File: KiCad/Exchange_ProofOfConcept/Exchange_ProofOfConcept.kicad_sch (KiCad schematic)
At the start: 21 parts, among them J1 Connector_PinHeader_2.54mm:Pi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, J2 Conn_01x02, J3 Conn_01x02, J4 Conn_01x02, J5 Connector_PinHeader_2.54mm:Pi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, J6 Connector_PinHeader_2.54mm:Pi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, J7 Screw_Terminal_01x02, J8 Conn_01x03, J9 Screw_Terminal_01x08, U1 MCP23017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

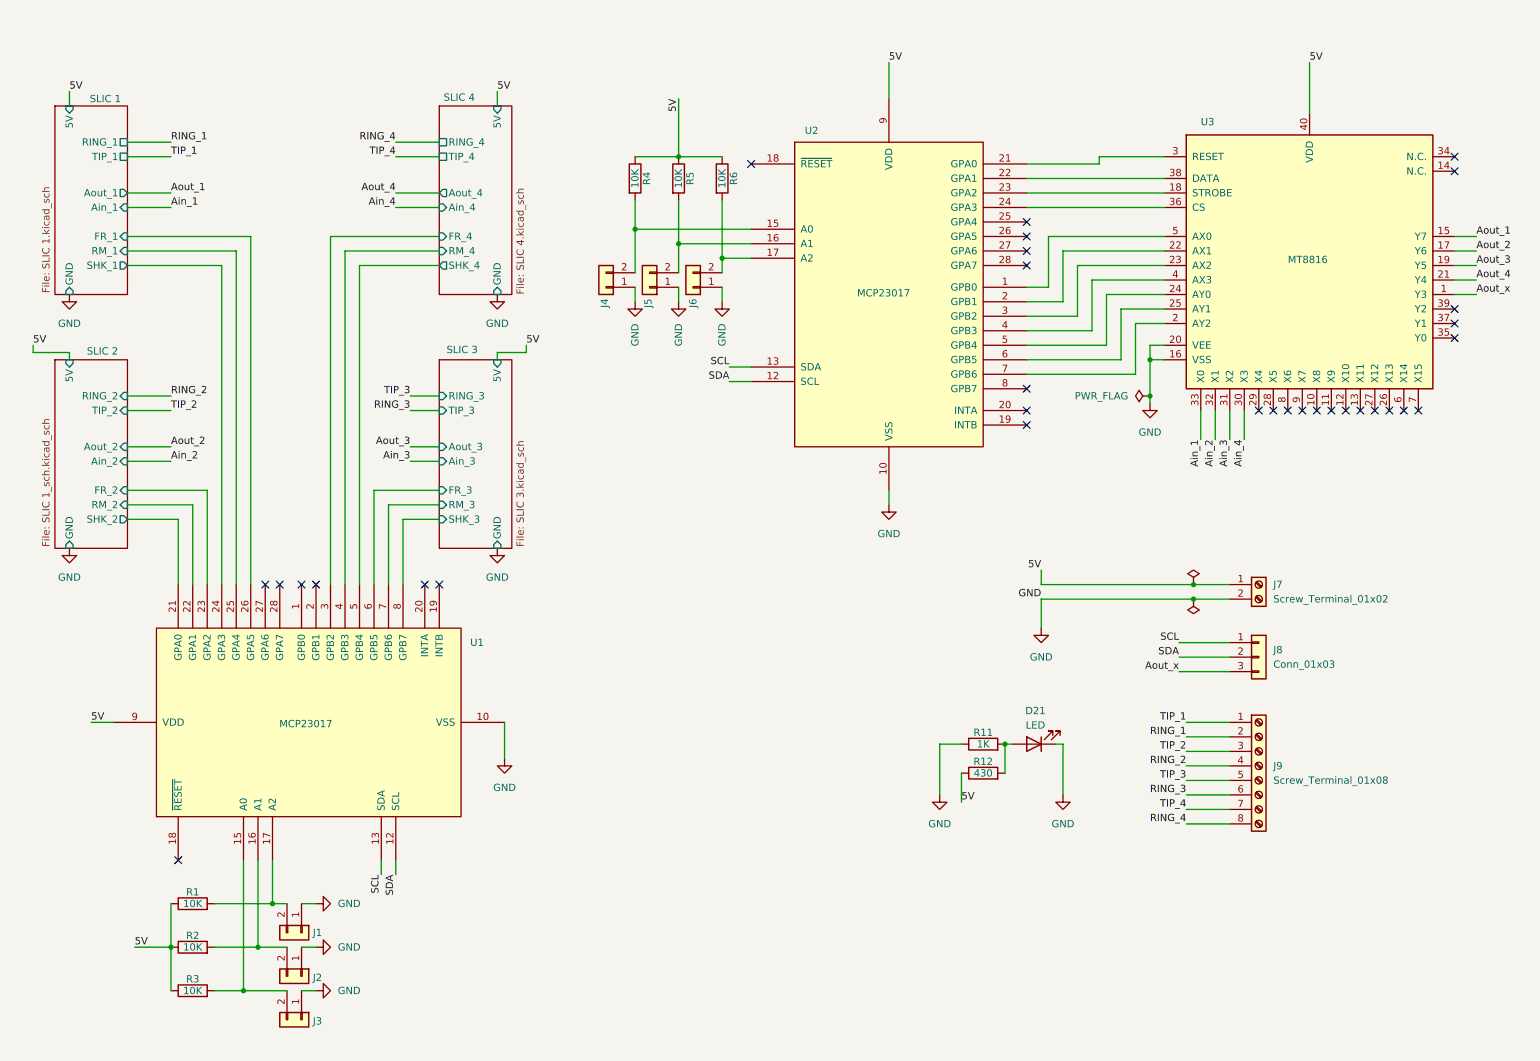
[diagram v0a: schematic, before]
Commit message: deleted:    KiCad/Exchange_ProofOfConcept/Exchange_ProofOfConcept-backups/Exchange_ProofOfConcept-2024-08-28_233227.zip 	deleted:    KiCad/Exchange_ProofOfConcept/Exchange_ProofOfConcept-backups/Exchange_ProofOfConcept-2024-08-28_234504.zip 	deleted:    KiCad/Exchange_ProofOfConcept/Exchange_ProofOfConcept-backups/Exchange_ProofOfConcept-2024-09-04_201626.zip 	deleted:    KiCad/Exchange_ProofOfConcept/Exchange_ProofOfConcept-backups/Exchange_ProofOfConcept-2024-09-04_202659.zip 	deleted:    KiCad/Exchange_ProofOfConcept/Exchange_ProofOfConcept-backups/Exchange_ProofOfConcept-2024-09-04_203703.zip 	deleted:    KiCad/Exchange_ProofOfConcept/Exchange_ProofOfConcept-backups/Exchange_ProofOfConcept-2024-09-04_204710.zip 	deleted:    KiCad/Exchange_ProofOfConcept/Exchange_ProofOfConcept-backups/Exchange_ProofOfConcept-2024-09-04_205754.zip 	deleted:    KiCad/Exchange_ProofOfConcept/Exchange_ProofOfConcept-backups/Exchange_ProofOfConcept-2024-09-05_153643.zip 	deleted:    KiCad/Exchange_ProofOfConcept/Exchange_ProofOfConcept-backups/Exchange_ProofOfConcept-2024-09-05_161017.zip 	deleted:    KiCad/Exchange_ProofOfConcept/Exchange_ProofOfConcept-backups/Exchange_ProofOfConcept-2024-09-05_162441.zip 	deleted:    KiCad/Exchange_ProofOfConcept/Exchange_ProofOfConcept-backups/Exchange_ProofOfConcept-2024-09-05_163641.zip 	deleted:    KiCad/Exchange_ProofOfConcept/Exchange_ProofOfConcept-backups/Exchange_ProofOfConcept-2024-09-06_180233.zip 	deleted:    KiCad/Exchange_ProofOfConcept/Exchange_ProofOfConcept-backups/Exchange_ProofOfConcept-2024-09-06_180943.zip 	deleted:    KiCad/Exchange_ProofOfConcept/Exchange_ProofOfConcept-backups/Exchange_ProofOfConcept-2024-09-06_182256.zip 	deleted:    KiCad/Exchange_ProofOfConcept/Exchange_ProofOfConcept-backups/Exchange_ProofOfConcept-2024-09-06_185314.zip 	deleted:    KiCad/Exchange_ProofOfConcept/Exchange_ProofOfConcept-backups/Exchange_ProofOfConcept-2024-09-06_191143.zip 	deleted:    KiCad/Exchange_ProofOfConcept/Exchange_ProofOfConcep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
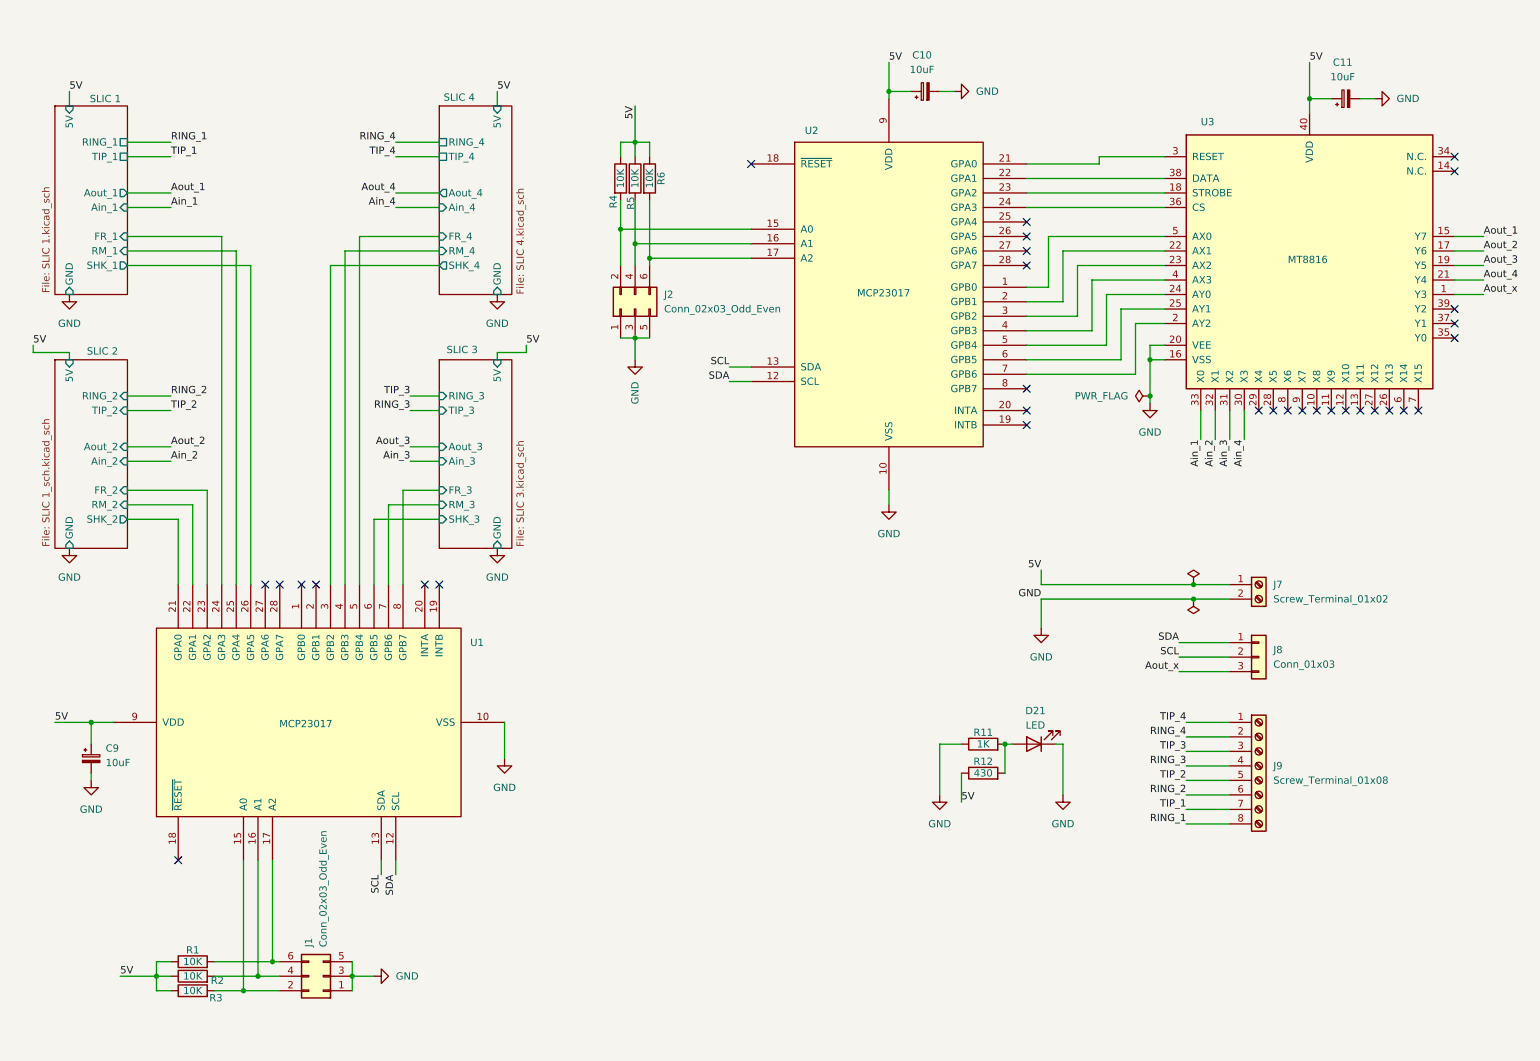
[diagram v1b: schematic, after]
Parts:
- removed J1, J5, J6: Connector_PinHeader_2.54mm:PinHeader_1x02_P2.54mm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, Connector_PinHeader_2.54mm:PinHeader_1x02_P2.54mm_Vertical, symbol Connector_Generic:Conn_01x02
- removed J2, J3, J4: Conn_01x02, Connector_PinHeader_2.54mm:PinHeader_1x02_P2.54mm_Vertical, symbol Connector_Generic:Conn_01x02
- added C10, C11, C9: 10uF, Capacitor_THT:CP_Radial_D4.0mm_P2.00mm, symbol Device:C_Polarized_Small
- added J1, J2: Conn_02x03_Odd_Even, Connector_PinHeader_2.54mm:PinHeader_2x03_P2.54mm_Vertical, symbol Connector_Generic:Conn_02x03_Odd_Even
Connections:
- net 5V: now also C10.1, C11.1, C9.1
- net GND: now also C10.2, C11.2, C9.2, J1.1 (Pin_1), J1.3 (Pin_3), J1.5 (Pin_5), J2.1 (Pin_1), J2.3 (Pin_3), J2.5 (Pin_5)
- net RING_1: now also J9.8 (Pin_8); no longer J9.2 (Pin_2)
- net RING_2: now also J9.6 (Pin_6); no longer J9.4 (Pin_4)
- net RING_3: now also J9.4 (Pin_4); no longer J9.6 (Pin_6)
- net RING_4: now also J9.2 (Pin_2); no longer J9.8 (Pin_8)
- net SCL: now also J8.2 (Pin_2); no longer J8.1 (Pin_1)
- net SDA: now also J8.1 (Pin_1); no longer J8.2 (Pin_2)
- net SLIC 1/FR_1: now also U1.24 (GPA3); no longer U1.26 (GPA5)
- net SLIC 1/SHK_1: now also U1.26 (GPA5); no longer U1.24 (GPA3)
- net SLIC 3/FR_3: now also U1.8 (GPB7); no longer U1.6 (GPB5)
- net SLIC 3/SHK_3: now also U1.6 (GPB5); no longer U1.8 (GPB7)
- net SLIC 4/FR_4: now also U1.5 (GPB4); no longer U1.3 (GPB2)
- net SLIC 4/SHK_4: now also U1.3 (GPB2); no longer U1.5 (GPB4)
- net TIP_1: now also J9.7 (Pin_7); no longer J9.1 (Pin_1)
- net TIP_2: now also J9.5 (Pin_5); no longer J9.3 (Pin_3)
- net TIP_3: now also J9.3 (Pin_3); no longer J9.5 (Pin_5)
- net TIP_4: now also J9.1 (Pin_1); no longer J9.7 (Pin_7)
- net at R2.2, U1.16 (A1): now also J1.4 (Pin_4)
- net at R3.2, U1.15 (A0): now also J1.2 (Pin_2)
- net at R5.2, U2.16 (A1): now also J2.4 (Pin_4)
- net at R4.2, U2.15 (A0): now also J2.2 (Pin_2)
- net at R1.2, U1.17 (A2): now also J1.6 (Pin_6)
- net at R6.2, U2.17 (A2): now also J2.6 (Pin_6)
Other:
- moved on the sheet: R4, R5, R6

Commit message: deleted:    KiCad/Exchange_ProofOfConcept/Exchange_ProofOfConcept-backups/Exchange_ProofOfConcept-2024-09-22_005249.zip 	new file:   KiCad/Exchange_ProofOfConcept/Exchange_ProofOfConcept-backups/Exchange_ProofOfConcept-2024-10-02_184119.zip 	modified:   KiCad/Exchange_ProofOfConcept/Exchange_ProofOfConcept.kicad_pcb 	modified:   KiCad/Exchange_ProofOfConcept/Exchange_ProofOfConcept.kicad_sch 	modified:   docs/PhoneStatusflowshart.drawio 	modified:   lib/LineStatusHandler/LineStatusHandler.cpp 	modified:   lib/LineStatusHandler/LineStatusHandler.h 	modified:   platformio.ini 	modified:   src/SHKRead.h 	modified:   src/config.h 	modified:   src/lineAction.h 	modified:   src/main.cpp
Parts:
- removed R11: 1K, Resistor_THT:R_Axial_DIN0204_L3.6mm_D1.6mm_P5.08mm_Horizontal, symbol Device:R
- R12: value 430 -> 470
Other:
- moved on the sheet: R12
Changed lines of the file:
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@@
 	)
 	(junction
-		(at 191.77 142.24)
-		(diameter 0)
-		(color 0 0 0 0)
-	)
-	(junction
 		(at 124.46 52.07)
 		(diameter 0)
@@
 	(wire
 		(pts
-			(xy 191.77 142.24) (xy 191.77 147.32)
-		)
-		(stroke
-			(width 0)
-			(type default)
-		)
-	)
-	(wire
-		(pts
 			(xy 129.54 57.15) (xy 147.32 57.15)
 		)
@@
 	(wire
 		(pts
-			(xy 180.34 142.24) (xy 180.34 151.13)
-		)
-		(stroke
-			(width 0)
-			(type default)
-		)
-	)
-	(wire
-		(pts
 			(xy 214.63 68.58) (xy 219.71 68.58)
 		)
@@
 	(wire
 		(pts
-			(xy 184.15 147.32) (xy 184.15 152.4)
+			(xy 180.34 142.24) (xy 180.34 156.21)
 		)
 		(stroke
@@
 	(wire
 		(pts
-			(xy 180.34 142.24) (xy 184.15 142.24)
+			(xy 87.63 83.82) (xy 92.71 83.82)
 		)
 		(stroke
@@
 	(wire
 		(pts
-			(xy 87.63 83.82) (xy 92.71 83.82)
+			(xy 143.51 76.2) (xy 147.32 76.2)
 		)
 		(stroke
@@
 	(wire
 		(pts
-			(xy 143.51 76.2) (xy 147.32 76.2)
+			(xy 231.14 83.82) (xy 231.14 88.9)
 		)
 		(stroke
@@
 	(wire
 		(pts
-			(xy 231.14 83.82) (xy 231.14 88.9)
+			(xy 198.12 114.3) (xy 224.79 114.3)
 		)
 		(stroke
@@
 	(wire
 		(pts
-			(xy 198.12 114.3) (xy 224.79 114.3)
+			(xy 223.52 138.43) (xy 231.14 138.43)
 		)
 		(stroke
@@
 	(wire
 		(pts
-			(xy 223.52 138.43) (xy 231.14 138.43)
+			(xy 180.34 142.24) (xy 184.15 142.24)
 		)
 		(stroke
@@
 	)
 	(label "5V"
-		(at 184.15 152.4 0)
+		(at 180.34 156.21 0)
 		(fields_autoplaced yes)
 		(effects
@@
 	(symbol
 		(lib_id "Device:R")
-		(at 187.96 147.32 90)
+		(at 187.96 142.24 90)
 		(unit 1)
 		(exclude_from_sim no)
@@
 		(dnp no)
 		(property "Reference" "R12"
-			(at 187.96 145.288 90)
+			(at 187.96 140.208 90)
 			(effects
 				(font
@@
 			)
 		)
-		(property "Value" "430"
-			(at 187.96 147.32 90)
+		(property "Value" "470"
+			(at 187.96 142.24 90)
 			(effects
 				(font
@@
 		)
 		(property "Footprint" "Resistor_THT:R_Axial_DIN0204_L3.6mm_D1.6mm_P5.08mm_Horizontal"
-			(at 187.96 149.098 90)
+			(at 187.96 144.018 90)
 			(effects
 				(font
@@
 		)
 		(property "Datasheet" "~"
-			(at 187.96 147.32 0)
+			(at 187.96 142.24 0)
 			(effects
 				(font
@@
 		)
 		(property "Description" "Resistor"
-			(at 187.96 147.32 0)
+			(at 187.96 142.24 0)
 			(effects
 				(font
@@
 	(symbol
 		(lib_id "Device:R")
-		(at 187.96 142.24 90)
-		(unit 1)
-		(exclude_from_sim no)
-		(in_bom yes)
-		(on_board yes)
-		(dnp no)
-		(property "Reference" "R11"
-			(at 187.96 140.208 90)
-			(effects
-				(font
-					(size 1.27 1.27)
-				)
-			)
-		)
-		(property "Value" "1K"
-			(at 187.96 142.24 90)
-			(effects
-				(font
-					(size 1.27 1.27)
-				)
-			)
-		)
-		(property "Footprint" "Resistor_THT:R_Axial_DIN0204_L3.6mm_D1.6mm_P5.08mm_Horizontal"
-			(at 187.96 144.018 90)
-			(effects
-				(font
-					(size 1.27 1.27)
-				)
-				(hide yes)
-			)
-		)
-		(property "Datasheet" "~"
-			(at 187.96 142.24 0)
-			(effects
-				(font
-					(size 1.27 1.27)
-				)
-				(hide yes)
-			)
-		)
-		(property "Description" "Resistor"
-			(at 187.96 142.24 0)
-			(effects
-				(font
-					(size 1.27 1.27)
-				)
-				(hide yes)
-			)
-		)
-		(pin "2"
-		)
-		(pin "1"
-		)
-		(instances
-			(project "Exchange_ProofOfConcept"
-				(path "/a3aa82f3-37b8-406c-999a-d11513c8e1fa"
-					(reference "R11")
-					(unit 1)
-				)
-			)
-		)
-	)
-	(symbol
-		(lib_id "Device:R")
 		(at 49.53 182.88 90)
 		(unit 1)
@@
 					(unit 1)
 				)
-			)
-		)
-	)
-	(symbol
-		(lib_id "power:GND")
-		(at 180.34 151.13 0)
-		(unit 1)
-		(exclude_from_sim no)
-		(in_bom yes)
-		(on_board yes)
-		(dnp no)
-		(fields_autoplaced yes)
-		(property "Reference" "#PWR025"
-			(at 180.34 157.48 0)
-			(effects
-				(font
-					(size 1.27 1.27)
-				)
-				(hide yes)
-			)
-		)
-		(property "Value" "GND"
-			(at 180.34 156.21 0)
-			(effects
-				(font
-					(size 1.27 1.27)
-				)
-			)
-		)
-		(property "Footprint" ""
-			(at 180.34 151.13 0)
-			(effects
-				(font
-					(size 1.27 1.27)
-				)
-				(hide yes)
-			)
-		)
-		(property "Datasheet" ""
-			(at 180.34 151.13 0)
-			(effects
-				(font
-					(size 1.27 1.27)
-				)
-				(hide yes)
-			)
-		)
-		(property "Description" "Power symbol creates a global label with name \"GND\" , ground"
-			(at 180.34 151.13 0)
-			(effects
-				(font
-					(size 1.27 1.27)
-				)
-				(hide yes)
-			)
-		)
-		(pin "1"
-		)
-		(instances
-			(project ""
-				(path "/a3aa82f3-37b8-406c-999a-d11513c8e1fa"
-					(reference "#PWR025")
-					(unit 1)
-				)

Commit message: new file:   KiCad/Exchange_ProofOfConcept/ESP-Unit/ESP-Unit-backups/ESP-Unit-2024-10-22_204833.zip 	new file:   KiCad/Exchange_ProofOfConcept/ESP-Unit/ESP-Unit-backups/ESP-Unit-2024-10-22_205851.zip 	new file:   KiCad/Exchange_ProofOfConcept/ESP-Unit/ESP-Unit-backups/ESP-Unit-2024-10-22_214835.zip 	new file:   KiCad/Exchange_ProofOfConcept/ESP-Unit/ESP-Unit-backups/ESP-Unit-2024-10-31_190638.zip 	new file:   KiCad/Exchange_ProofOfConcept/ESP-Unit/ESP-Unit.kicad_pcb 	new file:   KiCad/Exchange_ProofOfConcept/ESP-Unit/ESP-Unit.kicad_prl 	new file:   KiCad/Exchange_ProofOfConcept/ESP-Unit/ESP-Unit.kicad_pro 	new file:   KiCad/Exchange_ProofOfConcept/ESP-Unit/ESP-Unit.kicad_sch 	new file:   KiCad/Exchange_ProofOfConcept/ESP-Unit/fp-info-cache 	deleted:    KiCad/Exchange_ProofOfConcept/Exchange_ProofOfConcept-backups/Exchange_ProofOfConcept-2024-09-09_193050.zip 	deleted:    KiCad/Exchange_ProofOfConcept/Exchange_ProofOfConcept-backups/Exchange_ProofOfConcept-2024-09-10_220108.zip 	deleted:    KiCad/Exchange_ProofOfConcept/Exchange_ProofOfConcept-backups/Exchange_ProofOfConcept-2024-09-10_232037.zip 	deleted:    KiCad/Exchange_ProofOfConcept/Exchange_ProofOfConcept-backups/Exchange_ProofOfConcept-2024-09-11_034329.zip 	deleted:    KiCad/Exchange_ProofOfConcept/Exchange_ProofOfConcept-backups/Exchange_ProofOfConcept-2024-09-11_195456.zip 	deleted:    KiCad/Exchange_ProofOfConcept/Exchange_ProofOfConcept-backups/Exchange_ProofOfConcept-2024-09-17_174014.zip 	deleted:    KiCad/Exchange_ProofOfConcept/Exchange_ProofOfConcept-backups/Exchange_ProofOfConcept-2024-09-17_181112.zip 	deleted:    KiCad/Exchange_ProofOfConcept/Exchange_ProofOfConcept-backups/Exchange_ProofOfConcept-2024-09-19_202603.zip 	deleted:    KiCad/Exchange_ProofOfConcept/Exchange_ProofOfConcept-backups/Exchange_ProofOfConcept-2024-09-19_204637.zip 	deleted:    KiCad/Exchange_ProofOfConcept/Exchange_ProofOfConcept-backups/Exchange_ProofOfConcept-2024-09-19_205646.zip 	deleted:    KiCad/Exchange_ProofOfConcep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
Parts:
- removed J8: Conn_01x03, Connector_PinSocket_2.54mm:PinSocket_1x03_P2.54mm_Vertical, symbol Connector_Generic:Conn_01x03
- added C16, C17: 100nF, Capacitor_THT:C_Disc_D5.0mm_W2.5mm_P2.50mm, symbol Device:C
- added J3: Conn_01x04, Connector_PinSocket_2.54mm:PinSocket_1x04_P2.54mm_Vertical, symbol Connector_Generic:Conn_01x04
- added R11, R13: 10K, Resistor_THT:R_Axial_DIN0207_L6.3mm_D2.5mm_P7.62mm_Horizontal, symbol Device:R
- added R14, R15: 4,7K, Resistor_THT:R_Axial_DIN0207_L6.3mm_D2.5mm_P7.62mm_Horizontal, symbol Device:R
- R1, R12, R2, R3, R4, R5, R6: footprint Resistor_THT:R_Axial_DIN0204_L3.6mm_D1.6mm_P5.08mm_Horizontal -> Resistor_THT:R_Axial_DIN0207_L6.3mm_D2.5mm_P7.62mm_Horizontal
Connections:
- net 5V: now also C16.2, C17.1, R11.1, R13.2
- net Aout_x: now also J3.3 (Pin_3)
- net GND: now also C16.1, C17.2
- net SCL: now also J3.2 (Pin_2), R15.1
- net SDA: now also J3.1 (Pin_1), R14.1
- net at U1.18 (~{RESET}): now also R11.2
- net SLIC INT: now reaches U1.19 (INTB)
- net SLIC INT: now also U1.20 (INTA), J3.4 (Pin_4)
- net at U2.18 (~{RESET}): now also R13.1
- no-connect marks 32 -> 28
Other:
- moved on the sheet: C10, C11, C9, D21, J1, R1, R12, R2, R3, R4, R5, R6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
